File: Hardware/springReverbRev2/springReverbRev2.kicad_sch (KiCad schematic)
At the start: 16 parts, among them J907 Conn_01x08_Socket, J908 Conn_01x08_Pin, J909 Conn_01x09_Socket, J910 Conn_01x09_Pin, J911 2_pin_Molex_header, J912 2_pin_Molex_header, J913 2_pin_Molex_connector, J914 2_pin_Molex_connector

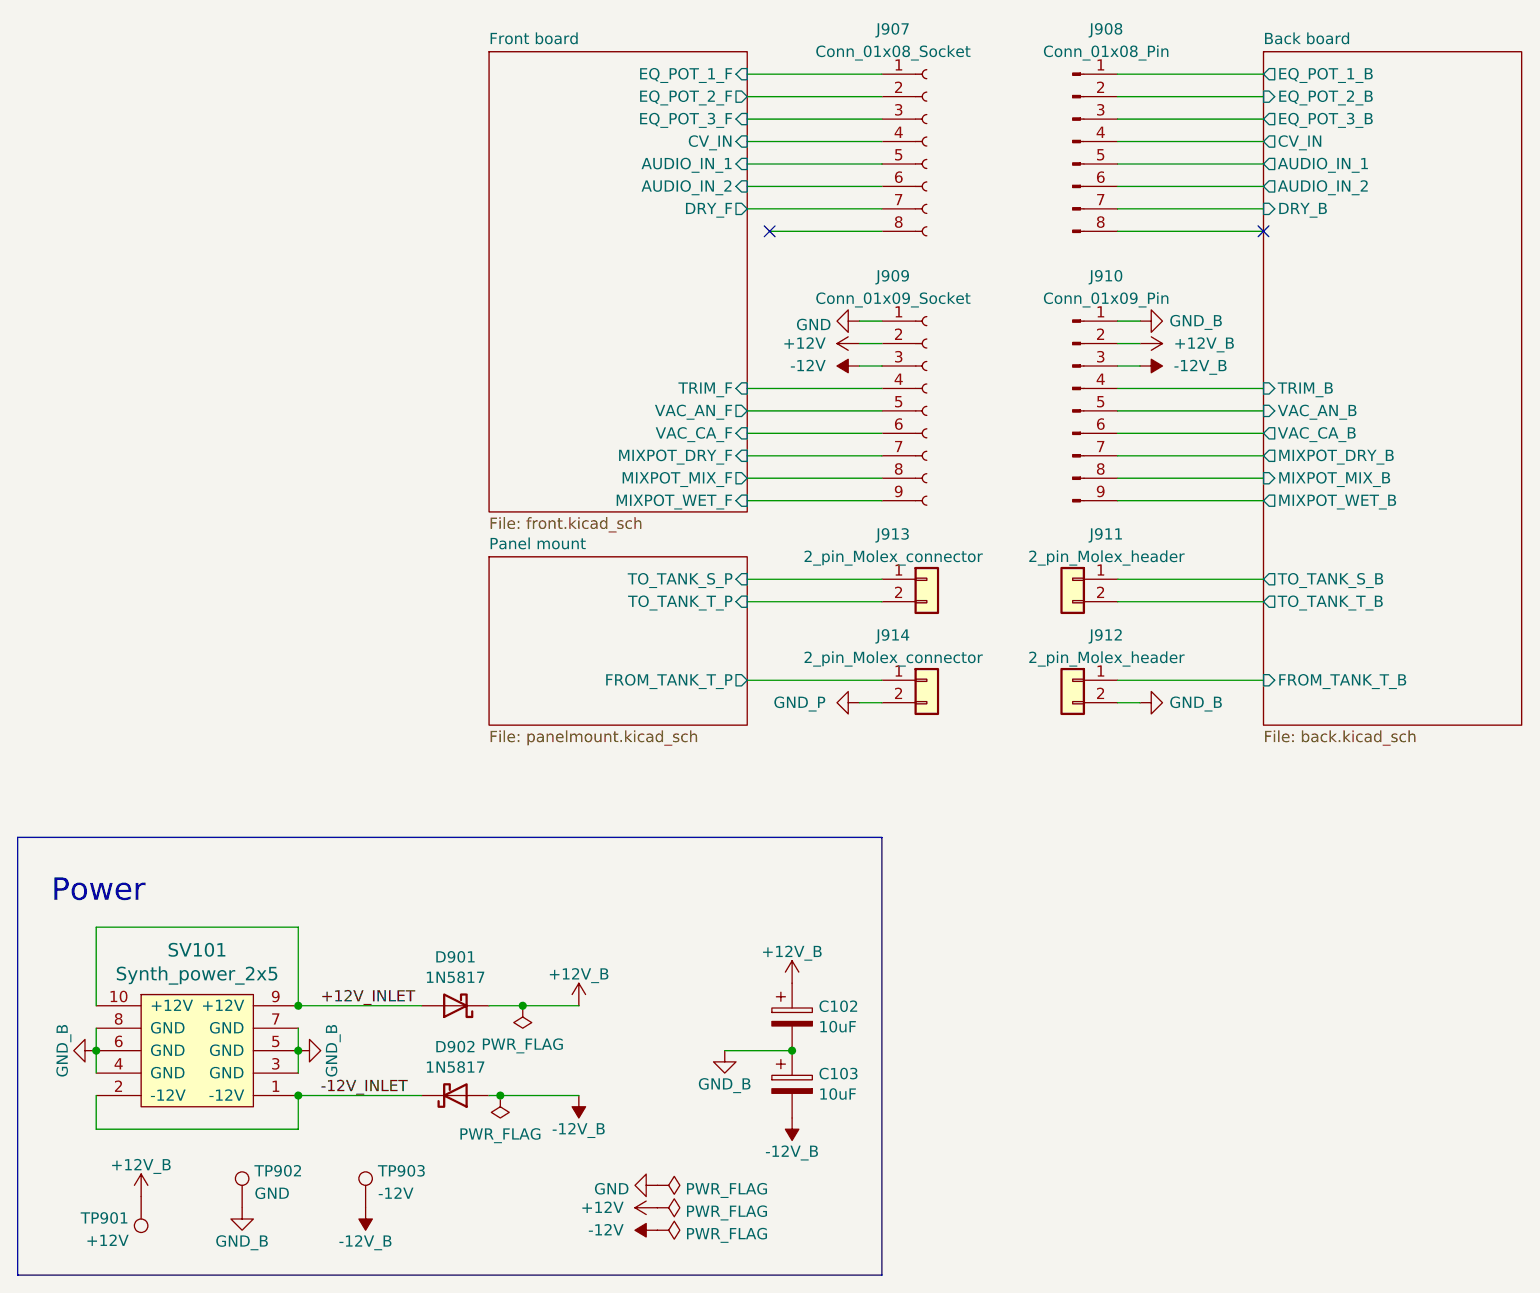
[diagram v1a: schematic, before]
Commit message: Docs; make LED position consistent
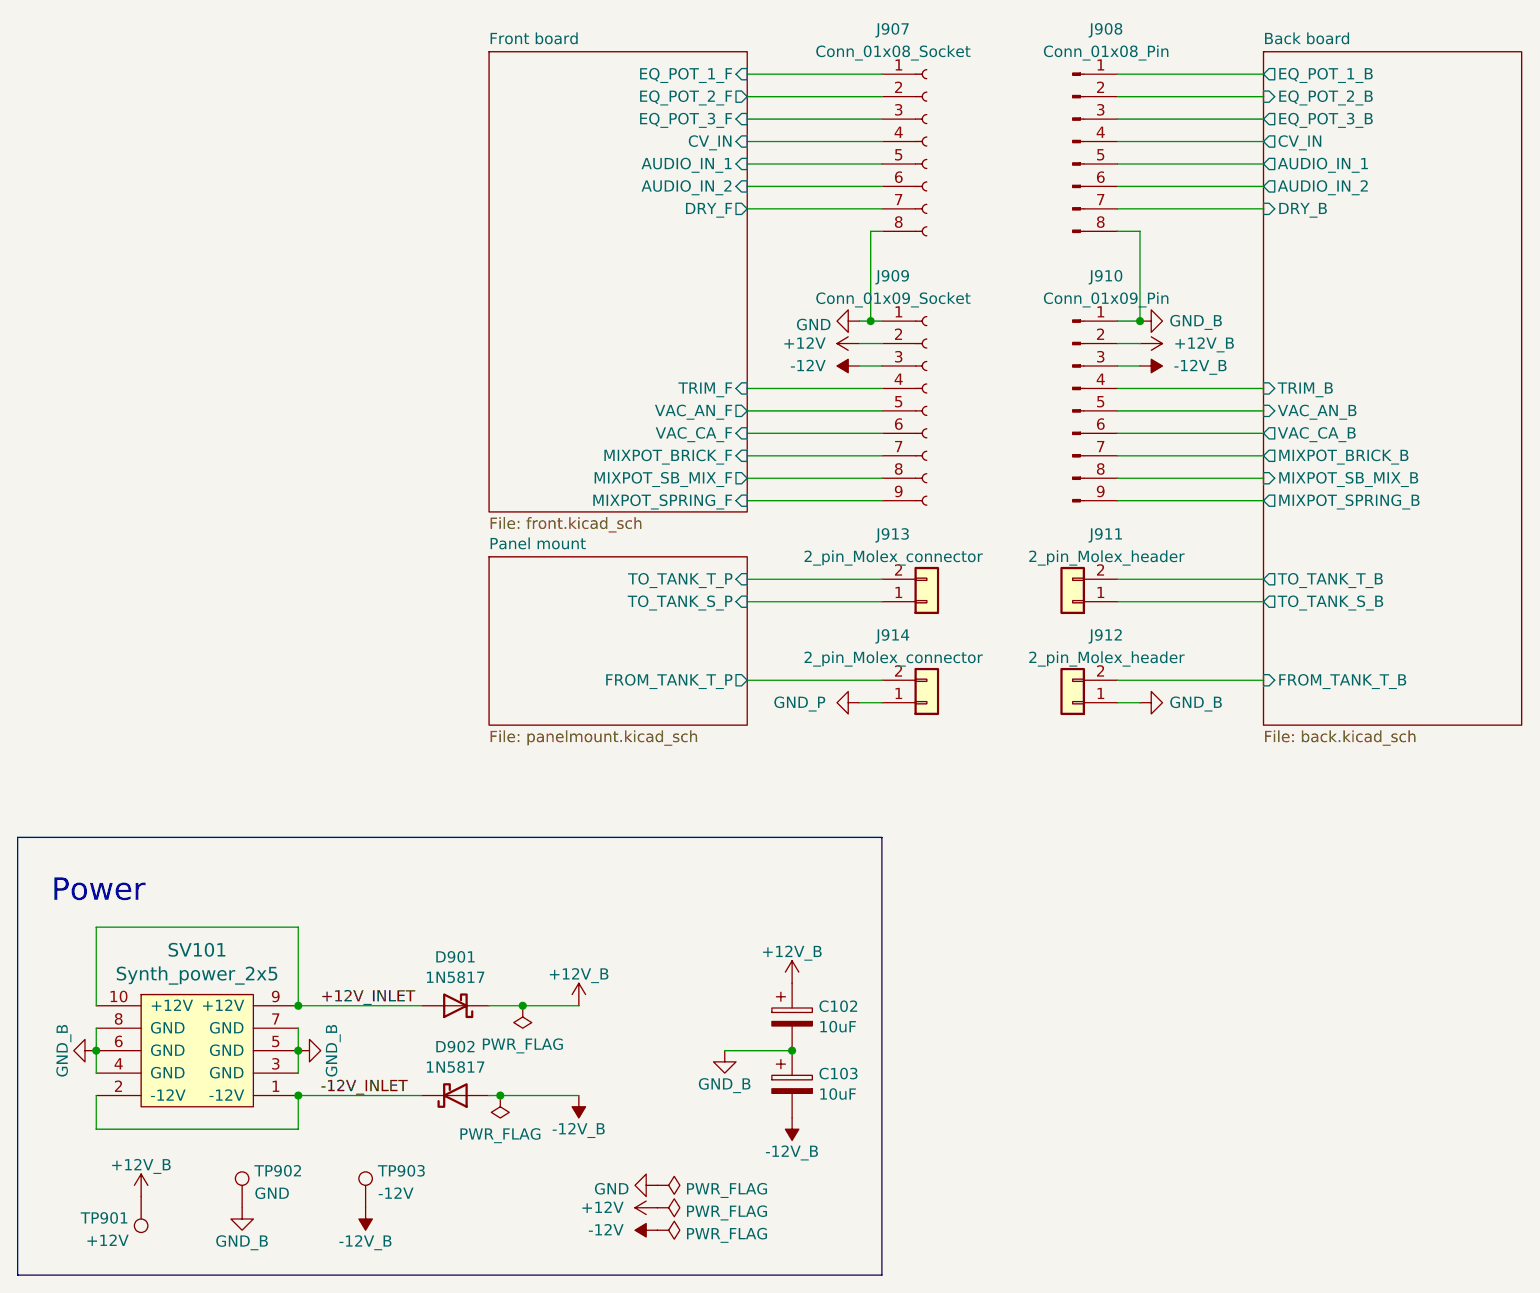
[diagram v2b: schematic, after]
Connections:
- net Back board/FROM_TANK_T_B: now also J912.2 (Pin_2); no longer J912.1 (Pin_1)
- net GND: now also J907.8 (Pin_8)
- net GND_B: now also J908.8 (Pin_8), J912.1 (Pin_1); no longer J912.2 (Pin_2)
- net GND_P: now also J914.1 (Pin_1); no longer J914.2 (Pin_2)
- net Panel mount/FROM_TANK_T_P: now also J914.2 (Pin_2); no longer J914.1 (Pin_1)
- net Back board/MIXPOT_DRY_B renamed Back board/MIXPOT_BRICK_B
- net Back board/MIXPOT_MIX_B renamed Back board/MIXPOT_SB_MIX_B
- net Back board/MIXPOT_WET_B renamed Back board/MIXPOT_SPRING_B
- net Front board/MIXPOT_DRY_F renamed Front board/MIXPOT_BRICK_F
- net Front board/MIXPOT_MIX_F renamed Front board/MIXPOT_SB_MIX_F
- net Front board/MIXPOT_WET_F renamed Front board/MIXPOT_SPRING_F
- no-connect marks 2 -> 0
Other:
- sheet Back board ports: added MIXPOT_BRICK_B, MIXPOT_SB_MIX_B, MIXPOT_SPRING_B; removed MIXPOT_DRY_B, MIXPOT_MIX_B, MIXPOT_WET_B
- sheet Front board ports: added MIXPOT_BRICK_F, MIXPOT_SB_MIX_F, MIXPOT_SPRING_F; removed MIXPOT_DRY_F, MIXPOT_MIX_F, MIXPOT_WET_F
- moved on the sheet: J911, J912
